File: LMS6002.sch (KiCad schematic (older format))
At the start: 53 parts, among them J1 SMA_H, J2 SMA_H, T1 B0322J5050, T2 B0322J5050, T3 TR_TC1-1-43X+, T4 TR_TC1-1-43X+, U12 BGS12, U13 BGS12, U3 LMS6002DR2

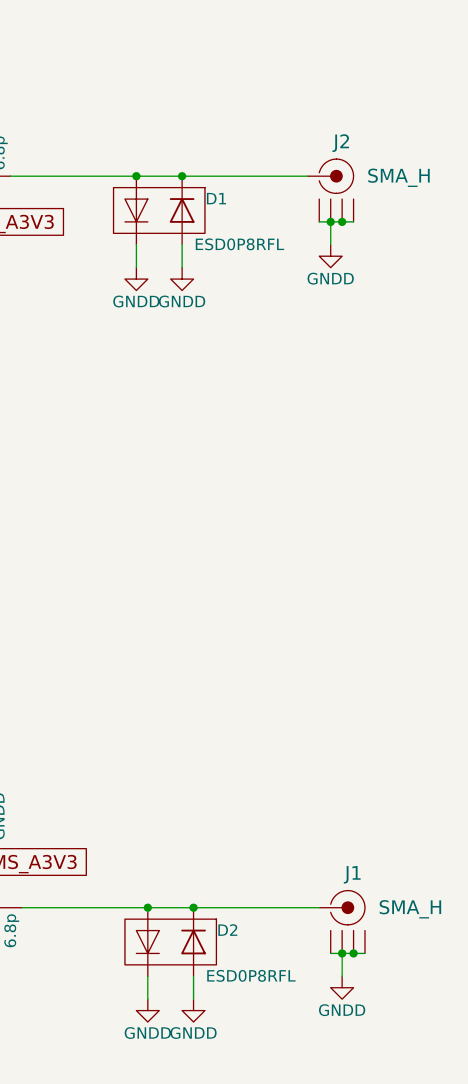
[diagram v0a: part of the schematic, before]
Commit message: Finish silkscreen layer.
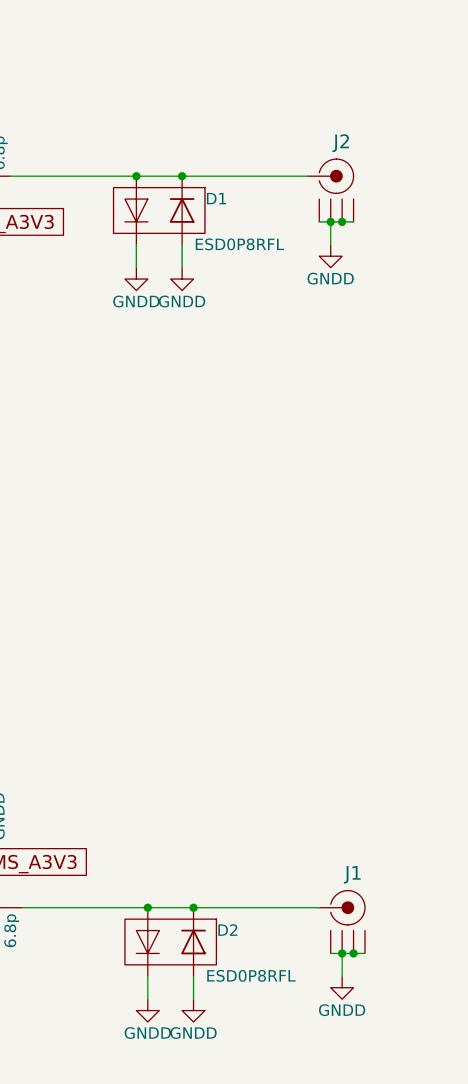
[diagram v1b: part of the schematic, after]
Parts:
- J1: value SMA_H -> RX; Component Value SMA_H -> (none)
- J2: value SMA_H -> TX; Component Value SMA_H -> (none)
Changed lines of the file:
@@
 P 10750 1900
 F 0 "J2" H 10750 2350 60  0000 C CNN
-F 1 "SMA_H" H 10650 2500 60  0001 C CNN
+F 1 "TX" H 10650 2500 60  0001 C CNN
 F 2 "sdr-foots:SMA_H" H 10650 2600 60  0001 C CNN
 F 3 "" H 10875 2215 60  0000 C CNN
@@
 F 7 "CON-SMA-EDGE-S" H 10650 2850 60  0001 C CNN "Manufacturer Part Number"
 F 8 "CONN, SMA, JACK, 50 OHM, EDGE MNT," H 10700 2700 60  0001 C CNN "Description"
-F 9 "SMA_H" H 11000 2200 60  0000 C CNN "Component Value"
 	1    10750 1900
 	1    0    0    -1
@@
 P 10800 5100
 F 0 "J1" H 10800 5550 60  0000 C CNN
-F 1 "SMA_H" H 10700 5700 60  0001 C CNN
+F 1 "RX" H 10700 5700 60  0001 C CNN
 F 2 "sdr-foots:SMA_H" H 10700 5800 60  0001 C CNN
 F 3 "" H 10925 5415 60  0000 C CNN
@@
 F 7 "CON-SMA-EDGE-S" H 10700 6050 60  0001 C CNN "Manufacturer Part Number"
 F 8 "CONN, SMA, JACK, 50 OHM, EDGE MNT," H 10750 5900 60  0001 C CNN "Description"
-F 9 "SMA_H" H 11050 5400 60  0000 C CNN "Component Value"
 	1    10800 5100
 	1    0    0    -1

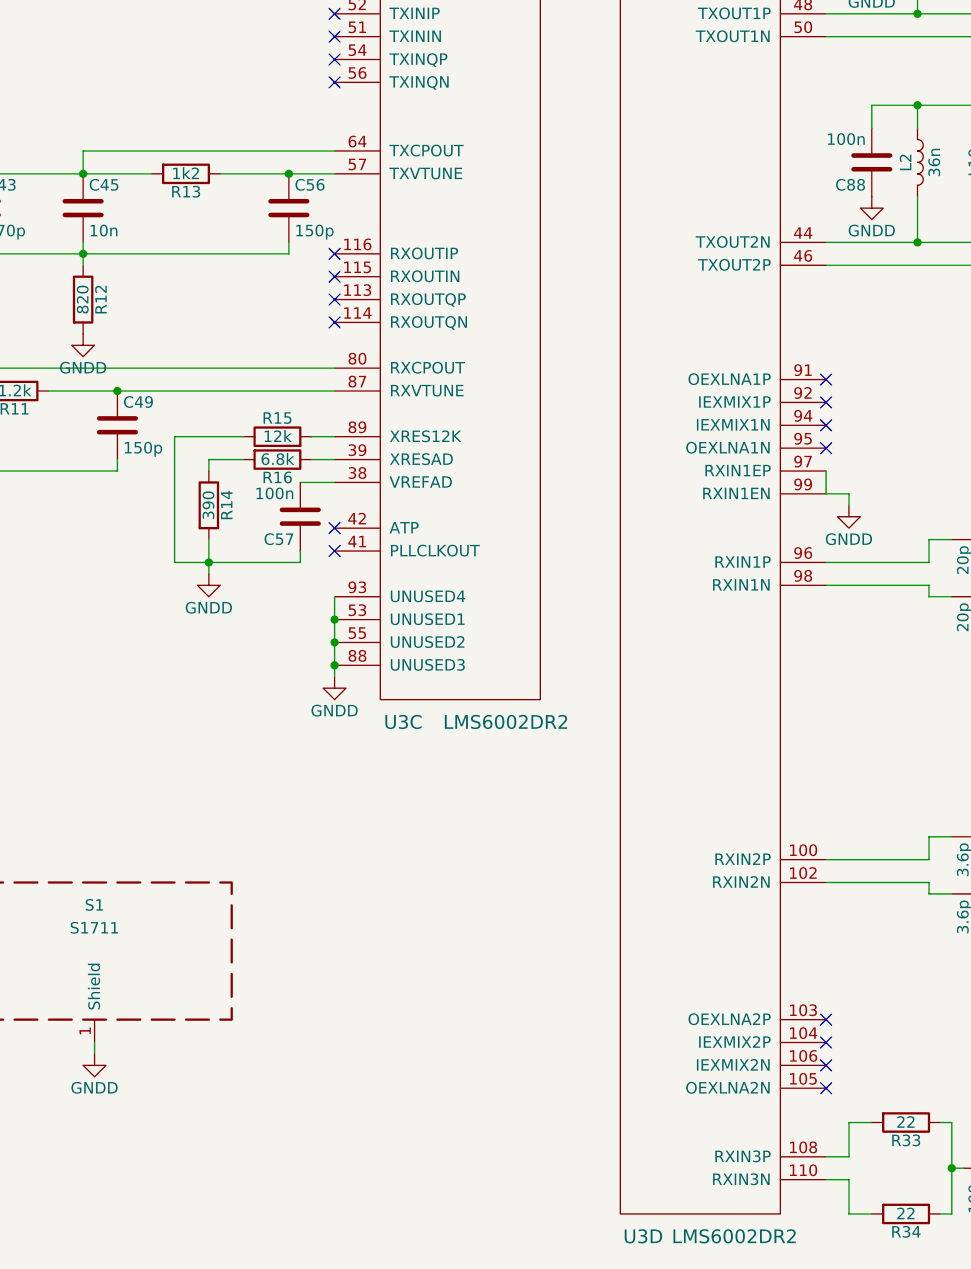
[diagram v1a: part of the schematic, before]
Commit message: Prepared BOM and changed some part numbers for unpopular ones. Added manufacture PN for each part.
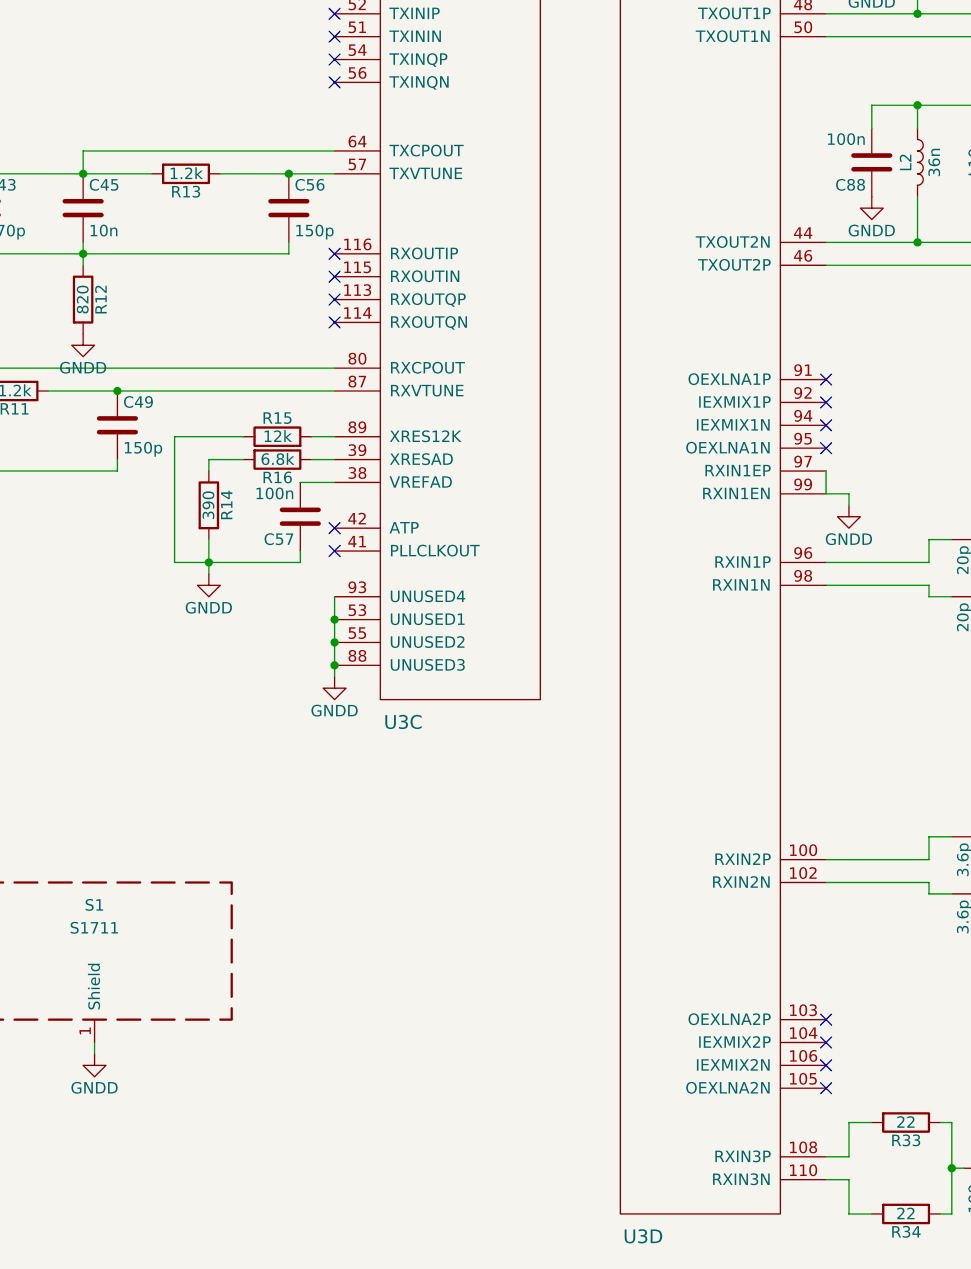
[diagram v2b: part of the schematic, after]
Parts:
- C41: manf# (none) -> C0603C471K3RACTU
- C42: manf# (none) -> GRM188R71E103KA01D
- C49: manf# (none) -> C0603C151K3GACTU
- C73: manf# (none) -> CBR06C689CAGAC
- C90: manf# (none) -> 251R14S200GV4T
- C97: manf# (none) -> GQM1885C2A3R6CB01D
- D1, D2: manf# (none) -> ESD0P8RFL
- J1, J2: Manufacturer RF Solutions -> Molex; Manufacturer Part Number CON-SMA-EDGE-S -> (none); Vendor Part Number J629-ND -> (none); manf# (none) -> 0732511150
- L2: manf# (none) -> LQW18AN36NG00D
- L8: manf# (none) -> AIMC-0603-2N7S-T
- R10: manf# (none) -> RC0603JR-07820RL
- R11: manf# (none) -> RC0603JR-071K2L
- R13: value 1k2 -> 1.2k; manf# (none) -> RC0603JR-071K2L
- R14: manf# (none) -> RC0603JR-07390RL
- R15: manf# (none) -> RC0603JR-0712KL
- R16: manf# (none) -> AC0603JR-076K8L
- S1: manf# (none) -> S1711-46R
- T1, T2: manf# (none) -> B0322J5050AHF
- T3: manf# (none) -> TR_TC1-1-43X+
- U12, U13: manf# (none) -> BGS12PL6
- U3: Component Value LMS6002DR2 -> (none); Vendor Digi-Key -> (none); Vendor Part Number 1434-1000-1-ND -> (none); manf# (none) -> LMS6002DFN
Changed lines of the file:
@@
 LIBS:valves
 LIBS:sdr
-LIBS:usb-type-c
 LIBS:sdr-cache
 EELAYER 25 0
@@
 F 2 "sdr-foots:DQFN-120_via_off_pad" H 4660 8850 60  0001 C CNN
 F 3 "" H 4700 6600 60  0000 C CNN
-F 4 "1434-1000-1-ND" H 4640 9360 60  0001 C CNN "Vendor Part Number"
-F 5 "Digi-Key" H 4630 9270 60  0001 C CNN "Vendor"
-F 6 "IC, MULTI-FUNCTION, TRANSCEIVER," H 4630 8940 60  0001 C CNN "Description"
-F 7 "Lime Microsystems Ltd" H 4640 9170 60  0001 C CNN "Manufacturer"
-F 8 "LMS6002DFN" H 4630 9050 60  0001 C CNN "Manufacturer Part Number"
-F 9 "LMS6002DR2" H 4800 6500 60  0000 C CNN "Component Value"
+F 4 "LMS6002DFN" H 4700 6600 60  0001 C CNN "manf#"
+F 5 "IC, MULTI-FUNCTION, TRANSCEIVER," H 4630 8940 60  0001 C CNN "Description"
+F 6 "Lime Microsystems Ltd" H 4640 9170 60  0001 C CNN "Manufacturer"
+F 7 "LMS6002DFN" H 4630 9050 60  0001 C CNN "Manufacturer Part Number"
 	4    4700 6600
 	1    0    0    -1
@@
 F 2 "sdr-foots:DQFN-120_via_off_pad" H 3560 6600 60  0001 C CNN
 F 3 "" H 3600 4350 60  0000 C CNN
-F 4 "1434-1000-1-ND" H 3540 7110 60  0001 C CNN "Vendor Part Number"
-F 5 "Digi-Key" H 3530 7020 60  0001 C CNN "Vendor"
-F 6 "IC, MULTI-FUNCTION, TRANSCEIVER," H 3530 6690 60  0001 C CNN "Description"
-F 7 "Lime Microsystems Ltd" H 3540 6920 60  0001 C CNN "Manufacturer"
-F 8 "LMS6002DFN" H 3530 6800 60  0001 C CNN "Manufacturer Part Number"
-F 9 "LMS6002DR2" H 3800 4250 60  0000 C CNN "Component Value"
+F 4 "LMS6002DFN" H 3600 4350 60  0001 C CNN "manf#"
+F 5 "IC, MULTI-FUNCTION, TRANSCEIVER," H 3530 6690 60  0001 C CNN "Description"
+F 6 "Lime Microsystems Ltd" H 3540 6920 60  0001 C CNN "Manufacturer"
+F 7 "LMS6002DFN" H 3530 6800 60  0001 C CNN "Manufacturer Part Number"
 	3    3600 4350
 	1    0    0    -1
@@
 F 2 "Capacitors_SMD:C_0603" H 788 3000 50  0001 C CNN
 F 3 "" H 750 3150 50  0000 C CNN
+F 4 "C0603C471K3RACTU" H 750 3150 60  0001 C CNN "manf#"
 	1    750  3150
 	1    0    0    -1
@@
 F 2 "Capacitors_SMD:C_0603" H 1238 3000 50  0001 C CNN
 F 3 "" H 1200 3150 50  0000 C CNN
+F 4 "GRM188R71E103KA01D" H 1200 3150 60  0001 C CNN "manf#"
 	1    1200 3150
 	1    0    0    -1
@@
 F 2 "Capacitors_SMD:C_0603" H 2138 3000 50  0001 C CNN
 F 3 "" H 2100 3150 50  0000 C CNN
+F 4 "C0603C151K3GACTU" H 2100 3150 60  0001 C CNN "manf#"
 	1    2100 3150
 	1    0    0    -1
@@
 F 2 "Resistors_SMD:R_0603" V 1130 3550 50  0001 C CNN
 F 3 "" H 1200 3550 50  0000 C CNN
+F 4 "RC0603JR-07820RL" H 1200 3550 60  0001 C CNN "manf#"
 	1    1200 3550
 	1    0    0    -1
@@
 F 2 "Resistors_SMD:R_0603" V 1580 3000 50  0001 C CNN
 F 3 "" H 1650 3000 50  0000 C CNN
+F 4 "RC0603JR-071K2L" H 1650 3000 60  0001 C CNN "manf#"
 	1    1650 3000
 	0    1    1    0
@@
 P 2400 2050
 F 0 "R13" V 2480 2050 50  0000 C CNN
-F 1 "1k2" V 2400 2050 50  0000 C CNN
+F 1 "1.2k" V 2400 2050 50  0000 C CNN
 F 2 "Resistors_SMD:R_0603" V 2330 2050 50  0001 C CNN
 F 3 "" H 2400 2050 50  0000 C CNN
+F 4 "RC0603JR-071K2L" H 2400 2050 60  0001 C CNN "manf#"
 	1    2400 2050
 	0    1    1    0
@@
 F 2 "Resistors_SMD:R_0603" V 2430 3500 50  0001 C CNN
 F 3 "" H 2500 3500 50  0000 C CNN
+F 4 "RC0603JR-07390RL" H 2500 3500 60  0001 C CNN "manf#"
 	1    2500 3500
 	1    0    0    -1
@@
 F 2 "Resistors_SMD:R_0603" V 2730 3300 50  0001 C CNN
 F 3 "" H 2800 3300 50  0000 C CNN
+F 4 "AC0603JR-076K8L" H 2800 3300 60  0001 C CNN "manf#"
 	1    2800 3300
 	0    1    1    0
@@
 F 2 "Resistors_SMD:R_0603" V 2730 3200 50  0001 C CNN
 F 3 "" H 2800 3200 50  0000 C CNN
+F 4 "RC0603JR-0712KL" H 2800 3200 60  0001 C CNN "manf#"
 	1    2800 3200
 	0    -1   -1   0
@@
 F 2 "Capacitors_SMD:C_0603" H 5938 3500 50  0001 C CNN
 F 3 "" H 5900 3650 50  0001 C CNN
+F 4 "251R14S200GV4T" H 5900 3650 60  0001 C CNN "manf#"
 	1    5900 3650
 	0    1    1    0
@@
 F 2 "Inductors_SMD:L_0603" H 6350 3650 50  0001 C CNN
 F 3 "" H 6350 3650 50  0001 C CNN
+F 4 "AIMC-0603-2N7S-T" H 6350 3650 60  0001 C CNN "manf#"
 	1    6350 3650
 	0    -1   -1   0
@@
 F 2 "sdr-foots:SMA_H" H 10650 2600 60  0001 C CNN
 F 3 "" H 10875 2215 60  0000 C CNN
-F 4 "Digi-Key" H 10650 3050 60  0001 C CNN "Vendor"
-F 5 "J629-ND" H 10650 3150 60  0001 C CNN "Vendor Part Number"
-F 6 "RF Solutions" H 10650 2950 60  0001 C CNN "Manufacturer"
-F 7 "CON-SMA-EDGE-S" H 10650 2850 60  0001 C CNN "Manufacturer Part Number"
-F 8 "CONN, SMA, JACK, 50 OHM, EDGE MNT," H 10700 2700 60  0001 C CNN "Description"
+F 4 "0732511150" H 10750 1900 60  0001 C CNN "manf#"
+F 5 "Digi-Key" H 10650 3050 60  0001 C CNN "Vendor"
+F 6 "Molex" H 10650 2950 60  0001 C CNN "Manufacturer"
+F 7 "CONN, SMA, JACK, 50 OHM, EDGE MNT," H 10700 2700 60  0001 C CNN "Description"
 	1    10750 1900
 	1    0    0    -1
@@
 F 2 "sdr-foots:B0322J5050" H 7325 1875 60  0001 C CNN
 F 3 "" H 7300 1640 60  0001 C CNN
-F 4 "Anaren" H 7350 2225 60  0001 C CNN "Manufacturer"
-F 5 "RF_Transformer;300_-_3000_MHz;_RF_Power_2_Watt;_Ratio_1:1;_50_Ohm;" H 7525 2000 60  0001 C CNN "Description"
-F 6 "B0322J5050AHF" H 7250 1650 60  0000 C CNN "Vendor Part Number"
-F 7 "B0322J5050" H 7300 1100 60  0001 C CNN "Component Value"
+F 4 "B0322J5050AHF" H 7300 1400 60  0001 C CNN "manf#"
+F 5 "Anaren" H 7350 2225 60  0001 C CNN "Manufacturer"
+F 6 "RF_Transformer;300_-_3000_MHz;_RF_Power_2_Watt;_Ratio_1:1;_50_Ohm;" H 7525 2000 60  0001 C CNN "Description"
+F 7 "B0322J5050AHF" H 7250 1650 60  0000 C CNN "Vendor Part Number"
+F 8 "B0322J5050" H 7300 1100 60  0001 C CNN "Component Value"
 	1    7300 1400
 	1    0    0    1
@@
 F 2 "sdr-foots:B0322J5050" H 7425 4275 60  0001 C CNN
 F 3 "" H 7400 4040 60  0001 C CNN
-F 4 "Anaren" H 7450 4625 60  0001 C CNN "Manufacturer"
-F 5 "RF_Transformer;300_-_3000_MHz;_RF_Power_2_Watt;_Ratio_1:1;_50_Ohm;" H 7625 4400 60  0001 C CNN "Description"
-F 6 "B0322J5050AHF" H 7900 3800 60  0000 C CNN "Vendor Part Number"
-F 7 "B0322J5050" H 7400 3500 60  0001 C CNN "Component Value"
+F 4 "B0322J5050AHF" H 7400 3800 60  0001 C CNN "manf#"
+F 5 "Anaren" H 7450 4625 60  0001 C CNN "Manufacturer"
+F 6 "RF_Transformer;300_-_3000_MHz;_RF_Power_2_Watt;_Ratio_1:1;_50_Ohm;" H 7625 4400 60  0001 C CNN "Description"
+F 7 "B0322J5050AHF" H 7900 3800 60  0000 C CNN "Vendor Part Number"
+F 8 "B0322J5050" H 7400 3500 60  0001 C CNN "Component Value"
 	1    7400 3800
 	1    0    0    1
@@
 F 2 "sdr-foots:TSLP-6-4" H 8200 2050 60  0001 C CNN
 F 3 "" H 8200 2050 60  0001 C CNN
+F 4 "BGS12PL6" H 8200 2050 60  0001 C CNN "manf#"
 	1    8200 2050
 	1    0    0    -1
@@
 F 2 "Capacitors_SMD:C_0603" H 6688 2350 50  0001 C CNN
 F 3 "" H 6650 2500 50  0001 C CNN
+F 4 "GQM1885C2A3R6CB01D" H 6650 2500 60  0001 C CNN "manf#"
 	1    6650 2500
 	0    1    1    0
@@
 F 2 "Inductors_SMD:L_0603" H 5600 2000 50  0001 C CNN
 F 3 "" H 5600 2000 50  0001 C CNN
+F 4 "LQW18AN36NG00D" H 5600 2000 60  0001 C CNN "manf#"
 	1    5600 2000
 	1    0    0    -1
@@
 F 2 "sdr-foots:TC1-1-43X+" H 7225 2875 60  0001 C CNN
 F 3 "" H 7200 2640 60  0000 C CNN
-F 4 "Mini-Circuits" H 7250 3225 60  0001 C CNN "Manufacturer"
-F 5 "RF_Transformer;_650_-_4000_MHz;_RF_Power_0.25_Watt;_Ratio_1:1;_50_Ohm;" H 7425 3000 60  0001 C CNN "Description"
-F 6 "TC1-1-43X+" H 7325 3125 60  0001 C CNN "Manufacturer Part Number"
-F 7 "TC1-1-43X+" H 7250 3450 60  0001 C CNN "Vendor Part Number"
-F 8 "TC1-1-43X+" H 7200 2100 60  0000 C CNN "Component Value"
+F 4 "TR_TC1-1-43X+" H 7200 2400 60  0001 C CNN "manf#"
+F 5 "Mini-Circuits" H 7250 3225 60  0001 C CNN "Manufacturer"
+F 6 "RF_Transformer;_650_-_4000_MHz;_RF_Power_0.25_Watt;_Ratio_1:1;_50_Ohm;" H 7425 3000 60  0001 C CNN "Description"
+F 7 "TC1-1-43X+" H 7325 3125 60  0001 C CNN "Manufacturer Part Number"
+F 8 "TC1-1-43X+" H 7250 3450 60  0001 C CNN "Vendor Part Number"
+F 9 "TC1-1-43X+" H 7200 2100 60  0000 C CNN "Component Value"
 	1    7200 2400
 	-1   0    0    -1
@@
 F 2 "sdr-foots:TSLP-4-7" H 10050 1750 50  0001 C CNN
 F 3 "" H 10050 1750 50  0001 C CNN
+F 4 "ESD0P8RFL" H 10050 1750 60  0001 C CNN "manf#"
 	1    10050 1750
 	0    1    1    0
@@
 F 2 "sdr-foots:SMA_H" H 10700 5800 60  0001 C CNN
 F 3 "" H 10925 5415 60  0000 C CNN
-F 4 "Digi-Key" H 10700 6250 60  0001 C CNN "Vendor"
-F 5 "J629-ND" H 10700 6350 60  0001 C CNN "Vendor Part Number"
-F 6 "RF Solutions" H 10700 6150 60  0001 C CNN "Manufacturer"
-F 7 "CON-SMA-EDGE-S" H 10700 6050 60  0001 C CNN "Manufacturer Part Number"
-F 8 "CONN, SMA, JACK, 50 OHM, EDGE MNT," H 10750 5900 60  0001 C CNN "Description"
+F 4 "0732511150" H 10800 5100 60  0001 C CNN "manf#"
+F 5 "Digi-Key" H 10700 6250 60  0001 C CNN "Vendor"
+F 6 "Molex" H 10700 6150 60  0001 C CNN "Manufacturer"
+F 7 "CONN, SMA, JACK, 50 OHM, EDGE MNT," H 10750 5900 60  0001 C CNN "Description"
 	1    10800 5100
 	1    0    0    -1
@@
 F 2 "sdr-foots:TSLP-6-4" H 8300 4350 60  0001 C CNN
 F 3 "" H 8300 4350 60  0001 C CNN
+F 4 "BGS12PL6" H 8300 4350 60  0001 C CNN "manf#"
 	1    8300 4350
 	1    0    0    1
@@
 F 2 "Capacitors_SMD:C_0603" H 9238 4650 50  0001 C CNN
 F 3 "" H 9200 4800 50  0001 C CNN
+F 4 "CBR06C689CAGAC" H 9200 4800 60  0001 C CNN "manf#"
 	1    9200 4800
 	0    -1   1    0
@@
 F 2 "sdr-foots:TSLP-4-7" H 10100 4950 50  0001 C CNN
 F 3 "" H 10100 4950 50  0001 C CNN
+F 4 "ESD0P8RFL" H 10100 4950 60  0001 C CNN "manf#"
 	1    10100 4950
 	0    1    1    0
@@
 F 2 "sdr-foots:SHIELD" H 2000 5350 50  0001 C CNN
 F 3 "" H 2000 5350 50  0001 C CNN
+F 4 "S1711-46R" H 2000 5450 60  0001 C CNN "manf#"
 	1    2000 5450
 	1    0    0    -1
